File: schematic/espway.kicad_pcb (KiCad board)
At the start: 2 copper layers, 43 x 33.2 mm, 36 parts, among them J1 CONN_01X02, J2 CONN_01X02, J3 CONN_01X04_MALE, SW1 SW_Push, U1 LM1117-3.3, U2 ESP-12E, U3 DRV8835, U4 LSM6DS3

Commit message: PCB adjustments
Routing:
- net Net-(R5-Pad2): track 21.8 -> 25.3 mm
- net Net-(R6-Pad2): track 21.7 -> 22.9 mm
- net +3V3: track 115.1 -> 115.9 mm
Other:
- net class Default: clearance 0.2 -> 0.16
- rule trace_clearance: 0.2 -> 0.16
- rule trace_min: 0.2 -> 0.16
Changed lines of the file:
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@@
     (links 80)
     (no_connects 0)
-    (area 119.843571 114 173.448301 157.148301)
+    (area 126.949999 121.199999 170.050001 154.550001)
     (thickness 1.6)
     (drawings 17)
-    (tracks 284)
+    (tracks 290)
     (zones 0)
     (modules 36)
@@
   (setup
     (last_trace_width 0.25)
+    (user_trace_width 0.17)
     (user_trace_width 0.5)
     (user_trace_width 0.75)
     (user_trace_width 1)
-    (trace_clearance 0.2)
+    (trace_clearance 0.16)
     (zone_clearance 0.4)
     (zone_45_only yes)
-    (trace_min 0.2)
+    (trace_min 0.16)
     (segment_width 0.2)
     (edge_width 0.1)
@@
   (net 29 "Net-(U4-Pad11)")
   (net_class Default "Tämä on oletuskytkentäverkkoluokka."
-    (clearance 0.2)
+    (clearance 0.16)
     (trace_width 0.25)
     (via_dia 0.6)
@@
   (segment (start 164.05 133.5) (end 164.25 133.5) (width 0.25) (layer F.Cu) (net 1))
   (segment (start 143.8 146.65) (end 143.8 146.9) (width 0.5) (layer F.Cu) (net 1))
+  (segment (start 158 134.5) (end 160 134.5) (width 0.25) (layer F.Cu) (net 2))
   (segment (start 148.8 148.75) (end 148.8 149.05) (width 0.25) (layer F.Cu) (net 2))
   (segment (start 148.8 147.5) (end 148.8 148.75) (width 0.25) (layer F.Cu) (net 2))
@@
   (segment (start 164.05 131) (end 164.325 131) (width 0.25) (layer F.Cu) (net 2))
   (segment (start 160 134.5) (end 159.8 134.5) (width 0.25) (layer F.Cu) (net 2))
-  (segment (start 159.8 134.5) (end 159.3 135) (width 0.25) (layer F.Cu) (net 2))
-  (segment (start 159.3 135) (end 158 135) (width 0.25) (layer F.Cu) (net 2))
   (segment (start 154.475001 136.975001) (end 156.024999 136.975001) (width 0.25) (layer F.Cu) (net 2))
   (segment (start 156.024999 136.975001) (end 158 135) (width 0.25) (layer F.Cu) (net 2))
@@
   (segment (start 146.85 146.05) (end 146.1 146.05) (width 0.25) (layer F.Cu) (net 2))
   (segment (start 146.85 145.55) (end 146.475 145.55) (width 0.25) (layer F.Cu) (net 2))
+  (segment (start 149 141) (end 149 132.784217) (width 0.25) (layer F.Cu) (net 3))
+  (segment (start 157.65 128.1) (end 159.3 129.75) (width 0.25) (layer F.Cu) (net 3))
+  (segment (start 149 132.784217) (end 153.684217 128.1) (width 0.25) (layer F.Cu) (net 3))
+  (segment (start 153.684217 128.1) (end 157.65 128.1) (width 0.25) (layer F.Cu) (net 3))
+  (segment (start 159.3 129.75) (end 160 129.75) (width 0.25) (layer F.Cu) (net 3))
+  (segment (start 135.974989 126.075011) (end 135.974989 127.674989) (width 0.17) (layer F.Cu) (net 3))
+  (segment (start 136.8 125.25) (end 135.974989 126.075011) (width 0.17) (layer F.Cu) (net 3))
+  (segment (start 137 125.25) (end 136.8 125.25) (width 0.17) (layer F.Cu) (net 3))
+  (segment (start 135.974989 127.674989) (end 136.8 128.5) (width 0.17) (layer F.Cu) (net 3))
+  (segment (start 135.7 143.75) (end 140.1 143.75) (width 0.5) (layer F.Cu) (net 3))
+  (segment (start 140.1 143.75) (end 141.5 145.15) (width 0.5) (layer F.Cu) (net 3))
+  (segment (start 141.5 145.15) (end 141.5 146.65) (width 0.5) (layer F.Cu) (net 3))
   (segment (start 148.8 145.1) (end 148.8 142.95) (width 0.25) (layer F.Cu) (net 3))
   (segment (start 148.8 142.95) (end 149 142.75) (width 0.25) (layer F.Cu) (net 3))
@@
   (segment (start 149.864998 144.1469) (end 149.864998 144.15) (width 0.25) (layer F.Cu) (net 3))
   (segment (start 149 143.281902) (end 149.864998 144.1469) (width 0.25) (layer F.Cu) (net 3))
-  (segment (start 137 125.75) (end 136.224999 126.525001) (width 0.25) (layer F.Cu) (net 3))
-  (segment (start 137 125.25) (end 137 125.75) (width 0.25) (layer F.Cu) (net 3))
-  (segment (start 136.224999 126.525001) (end 136.224999 127.924999) (width 0.25) (layer F.Cu) (net 3))
-  (segment (start 136.224999 127.924999) (end 136.8 128.5) (width 0.25) (layer F.Cu) (net 3))
   (segment (start 137 137.1) (end 137 137.75) (width 0.25) (layer F.Cu) (net 3))
   (segment (start 137 134.285002) (end 137 137.1) (width 0.25) (layer F.Cu) (net 3))
@@
   (segment (start 154.00783 149.19217) (end 154.00783 147.722828) (width 0.25) (layer F.Cu) (net 3))
   (segment (start 154.00783 147.722828) (end 154 147.714998) (width 0.25) (layer F.Cu) (net 3))
-  (segment (start 149 141) (end 149 130.765) (width 0.25) (layer F.Cu) (net 3))
-  (segment (start 151.665 128.1) (end 158.15 128.1) (width 0.25) (layer F.Cu) (net 3))
-  (segment (start 158.15 128.1) (end 159.8 129.75) (width 0.25) (layer F.Cu) (net 3))
-  (segment (start 149 130.765) (end 151.665 128.1) (width 0.25) (layer F.Cu) (net 3))
-  (segment (start 159.8 129.75) (end 160 129.75) (width 0.25) (layer F.Cu) (net 3))
   (segment (start 149 142.75) (end 149 141) (width 0.25) (layer F.Cu) (net 3))
   (segment (start 147.75 149.5) (end 147.775 149.5) (width 0.25) (layer F.Cu) (net 3))
@@
   (segment (start 139.6 143.75) (end 141.5 141.85) (width 0.5) (layer F.Cu) (net 3))
   (segment (start 141.5 141.85) (end 141.5 140.35) (width 0.5) (layer F.Cu) (net 3))
-  (segment (start 141.5 146.65) (end 141.5 140.35) (width 0.5) (layer F.Cu) (net 3))
   (segment (start 141.5 140.35) (end 141.5 138) (width 0.5) (layer F.Cu) (net 3))
   (segment (start 141.5 138) (end 140.475001 136.975001) (width 0.5) (layer F.Cu) (net 3))
@@
   (segment (start 160.974999 130.674999) (end 161.3 131) (width 0.25) (layer F.Cu) (net 14))
   (segment (start 161.3 131) (end 161.95 131) (width 0.25) (layer F.Cu) (net 14))
-  (segment (start 136.25 130.25) (end 136.5 130.5) (width 0.25) (layer F.Cu) (net 15))
-  (segment (start 136.5 130.5) (end 138.2 128.8) (width 0.25) (layer F.Cu) (net 15))
-  (segment (start 138.2 128.8) (end 138.2 128.202912) (width 0.25) (layer F.Cu) (net 15))
-  (segment (start 138.2 128.202912) (end 138.535242 127.86767) (width 0.25) (layer F.Cu) (net 15))
-  (segment (start 138.535242 127.86767) (end 148.88233 127.86767) (width 0.25) (layer F.Cu) (net 15))
-  (segment (start 148.88233 127.86767) (end 153.774999 122.975001) (width 0.25) (layer F.Cu) (net 15))
-  (segment (start 153.774999 122.975001) (end 154.475001 122.975001) (width 0.25) (layer F.Cu) (net 15))
-  (segment (start 136.25 132.05) (end 138.449998 129.850002) (width 0.25) (layer F.Cu) (net 16))
-  (segment (start 153.524999 124.975001) (end 154.475001 124.975001) (width 0.25) (layer F.Cu) (net 16))
-  (segment (start 148.649998 129.850002) (end 153.524999 124.975001) (width 0.25) (layer F.Cu) (net 16))
-  (segment (start 138.449998 129.850002) (end 148.649998 129.850002) (width 0.25) (layer F.Cu) (net 16))
+  (segment (start 154.475001 122.975001) (end 151.459757 125.990245) (width 0.17) (layer F.Cu) (net 15))
+  (segment (start 136.304999 127.446001) (end 136.585631 127.726633) (width 0.17) (layer F.Cu) (net 15))
+  (segment (start 151.459757 125.990245) (end 136.82359 125.990245) (width 0.17) (layer F.Cu) (net 15))
+  (segment (start 136.304999 126.508836) (end 136.304999 127.446001) (width 0.17) (layer F.Cu) (net 15))
+  (segment (start 136.585631 127.726633) (end 137.367635 127.726633) (width 0.17) (layer F.Cu) (net 15))
+  (segment (start 137.695001 128.053999) (end 137.695001 128.854999) (width 0.17) (layer F.Cu) (net 15))
+  (segment (start 136.25 130.3) (end 136.25 130.5) (width 0.17) (layer F.Cu) (net 15))
+  (segment (start 136.82359 125.990245) (end 136.304999 126.508836) (width 0.17) (layer F.Cu) (net 15))
+  (segment (start 137.695001 128.854999) (end 136.25 130.3) (width 0.17) (layer F.Cu) (net 15))
+  (segment (start 137.367635 127.726633) (end 137.695001 128.053999) (width 0.17) (layer F.Cu) (net 15))
+  (segment (start 136.25 132.25) (end 136.25 131.761686) (width 0.17) (layer F.Cu) (net 16))
+  (segment (start 136.25 131.761686) (end 138.131735 129.879951) (width 0.17) (layer F.Cu) (net 16))
+  (segment (start 138.131735 128.377265) (end 138.573902 127.935098) (width 0.17) (layer F.Cu) (net 16))
+  (segment (start 138.573902 127.935098) (end 151.514904 127.935098) (width 0.17) (layer F.Cu) (net 16))
+  (segment (start 151.514904 127.935098) (end 154.475001 124.975001) (width 0.17) (layer F.Cu) (net 16))
+  (segment (start 138.131735 129.879951) (end 138.131735 128.377265) (width 0.17) (layer F.Cu) (net 16))
   (segment (start 136.25 132.25) (end 136.25 132.05) (width 0.25) (layer F.Cu) (net 16))
   (segment (start 154.153589 124.975001) (end 154.475001 124.975001) (width 0.25) (layer F.Cu) (net 16))

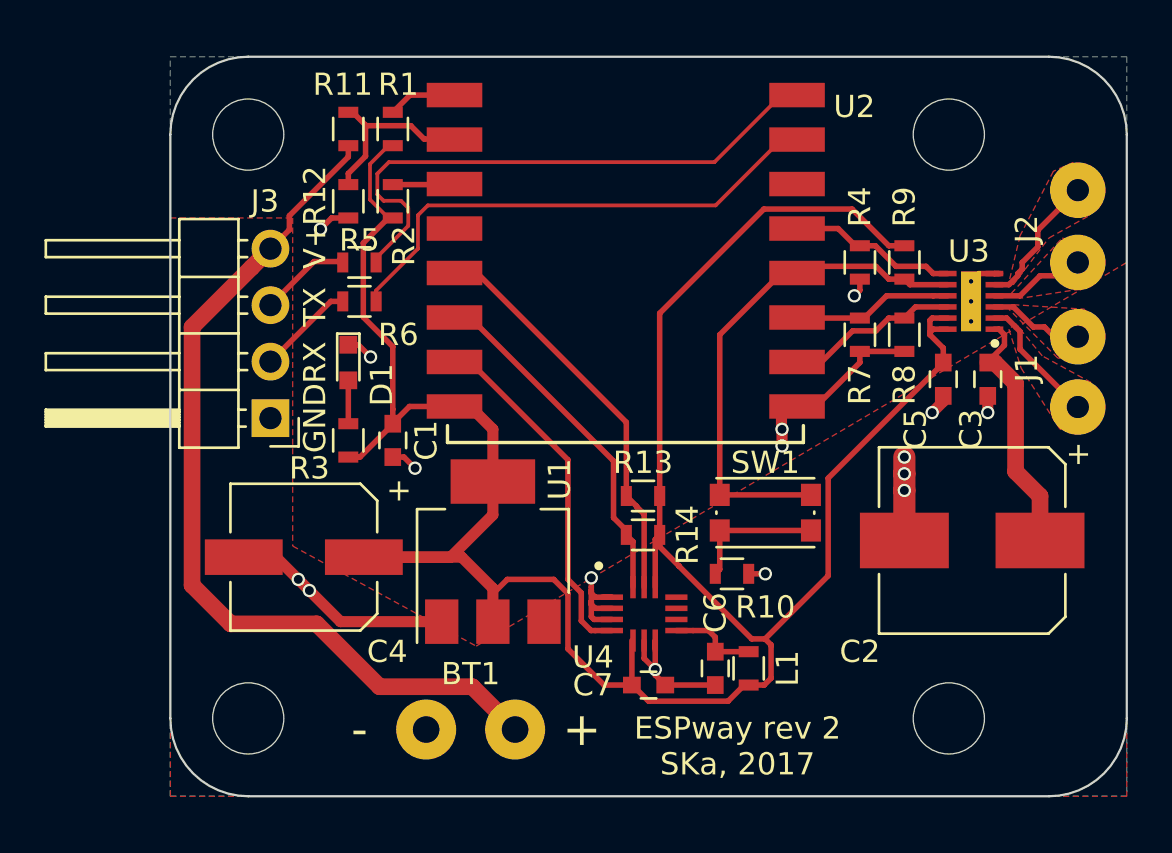
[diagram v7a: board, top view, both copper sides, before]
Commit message: PCB: reflect the previous schematic changes
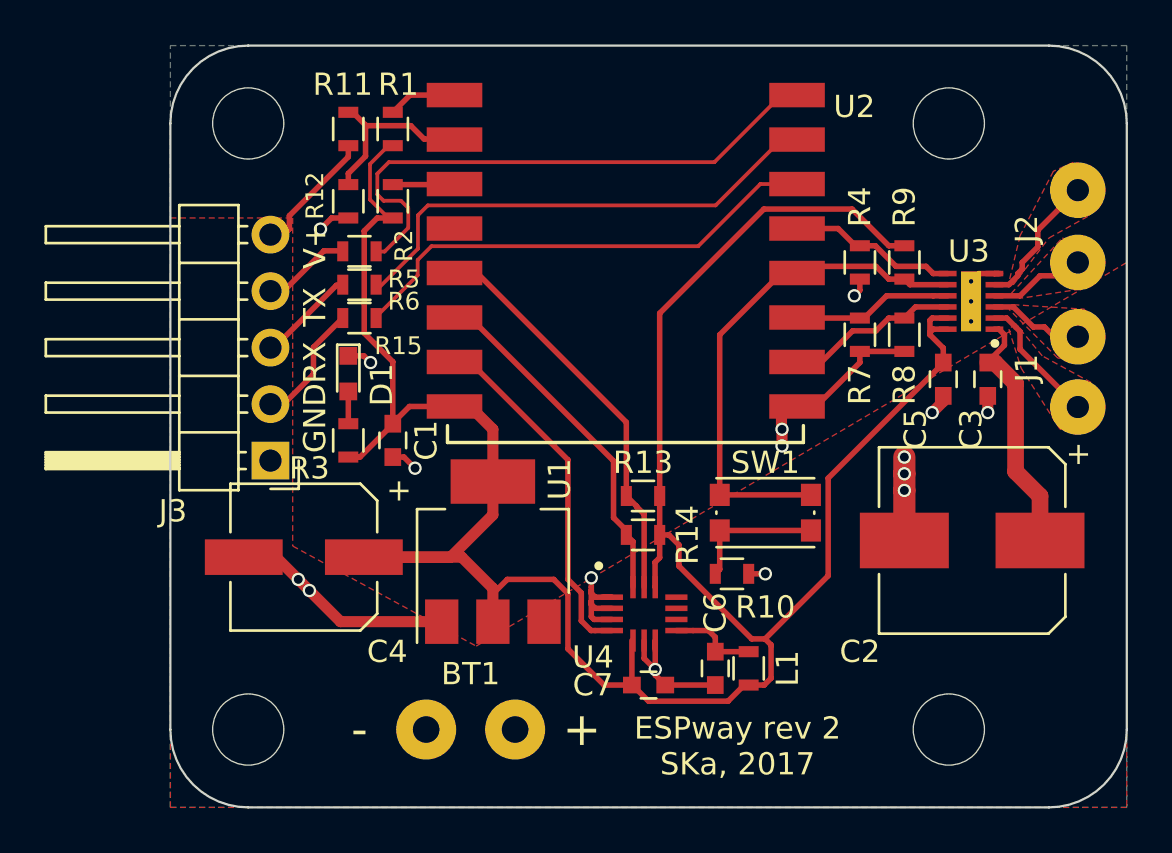
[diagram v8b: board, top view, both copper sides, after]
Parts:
- added R15: 100, Resistors_SMD:R_0603, F.Cu at (135.5, 133.0)
- J3: value CONN_01X04_MALE -> Conn_01x05_Male; footprint Pin_Headers:Pin_Header_Angled_1x04_Pitch2.54mm -> Pin_Headers:Pin_Header_Angled_1x05_Pitch2.54mm
- R10, R3, R5, R6: value 470 -> 100
- moved J3 1.91 mm to (131.5, 139.4)
- moved R6 0.75 mm to (135.5, 131.5)
- moved D1 0.50 mm to (135.0, 135.5)
- moved R5 0.50 mm to (135.5, 130.0)
- moved REF** 0.50 mm to (162.0, 151.5)
- moved REF** 0.50 mm to (130.5, 151.5)
- moved REF** 0.50 mm to (162.0, 124.2)
- moved REF** 0.50 mm to (130.5, 124.2)
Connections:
- J3 pad 4: +BATT -> Net-(J3-Pad4)
- R5 pad 1: Net-(J3-Pad3) -> Net-(J3-Pad4)
- R6 pad 1: Net-(J3-Pad2) -> Net-(J3-Pad3)
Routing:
- net +BATT: track 51.7 -> 17.8 mm
- net Net-(R15-Pad2): track 0.00 -> 21.2 mm
- net Net-(J3-Pad4): track 0.00 -> 4.22 mm
- net Net-(J3-Pad2): track 4.37 -> 5.81 mm
- net +3V3: track 115.9 -> 116.6 mm
- net Net-(J3-Pad3): track 4.15 -> 4.86 mm
- net Net-(R6-Pad2): track 22.9 -> 22.2 mm
- net Net-(D1-Pad2): track 1.95 -> 1.45 mm
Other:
- board size 43 x 33.2 mm -> 43 x 34.2 mm
